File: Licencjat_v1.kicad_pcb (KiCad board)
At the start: 2 copper layers, 53 parts, among them J1 Conn_01x02_Socket, J2 Conn_01x02_Socket, J3 Conn_01x04_Socket, J4 Conn_01x05_Socket, J5 Conn_01x04_Socket, J6 Conn_01x04_Socket, J7 AVR-ISP-6, Q1 AO3401A, Q10 2SC1945, Q2 BC846, Q3 AO3401A, Q4 AO3401A, Q8 AO3401A, Q9 2SC1945, U1 ATmega328P-A, U2 XC6206PxxxMR, U3 HT75xx-1-SOT89, Y1 Crystal_Small

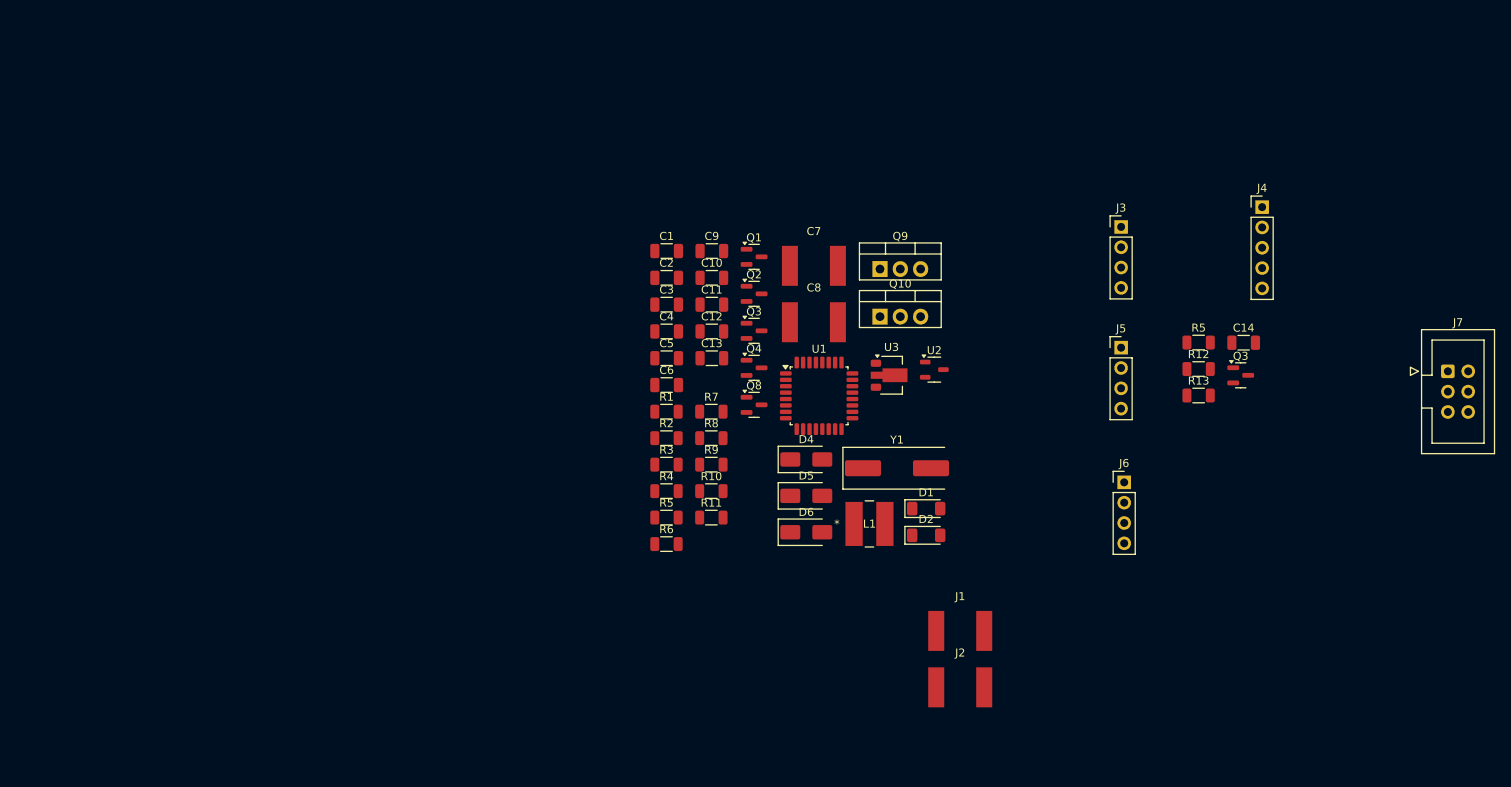
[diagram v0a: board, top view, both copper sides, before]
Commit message: Add 1Wire, RF Level SHifter and better footprints
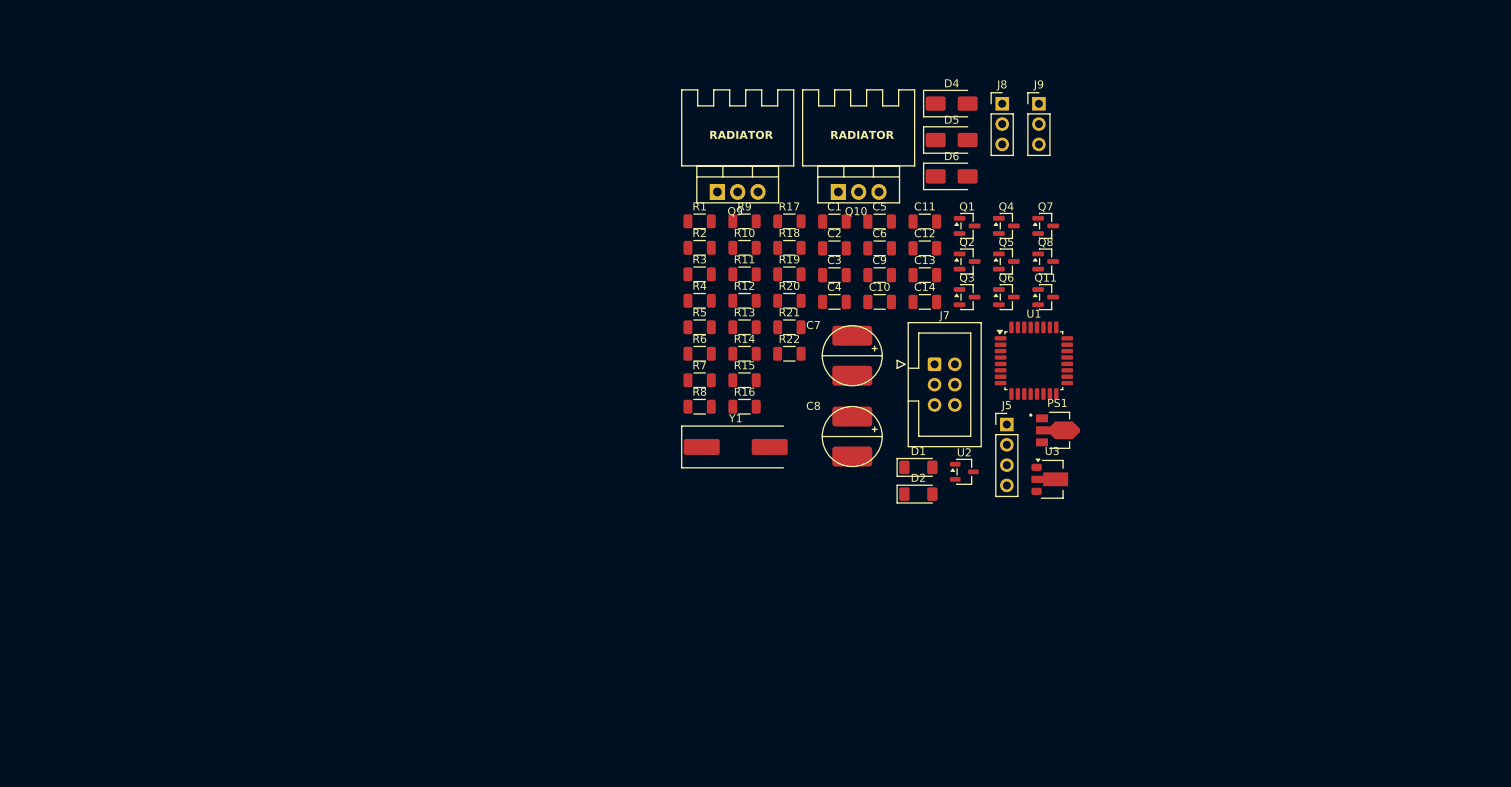
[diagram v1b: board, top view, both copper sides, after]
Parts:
- removed J1, J2: Conn_01x02_Socket, foot_prints:DoubleSolderWirePad_1x01_SMD_2x5mm
- removed J3: Conn_01x04_Socket, foot_prints:ATH20 + BMP280
- removed J4: Conn_01x05_Socket, foot_prints:VEML7700
- removed J6: Conn_01x04_Socket, foot_prints:RF_TRANSMITTER
- removed L1: L, Inductor cd54:IND_CD54_SUM
- removed the Q3 at (163.1, 61.0)
- removed the Q3 at (102.2, 55.4)
- removed the R5 at (157.8, 56.9)
- removed the R5 at (91.3, 78.8)
- added J8: GEIGER, Connector_PinHeader_2.54mm:PinHeader_1x03_P2.54mm_Vertical, F.Cu at (133.2, 27.1)
- added J9: 1_WIRE, Connector_PinHeader_2.54mm:PinHeader_1x03_P2.54mm_Vertical, F.Cu at (137.8, 27.1)
- added PS1: ME2108A33P, ME2108A33P:CONV_ME2108A33P, F.Cu at (140.2, 67.9)
- added Q11: AO3400A, Package_TO_SOT_SMD:SOT-23, F.Cu at (138.7, 51.2)
- added Q3: AO3401A, Package_TO_SOT_SMD:SOT-23, F.Cu at (128.9, 51.2)
- added Q5: AO3400A, Package_TO_SOT_SMD:SOT-23, F.Cu at (133.8, 46.8)
- added Q6: AO3400A, Package_TO_SOT_SMD:SOT-23, F.Cu at (133.8, 51.2)
- added Q7: AO3401A, Package_TO_SOT_SMD:SOT-23, F.Cu at (138.7, 42.3)
- added R14: 10k, Resistor_SMD:R_1206_3216Metric, F.Cu at (101.0, 58.3)
- added R15: 10k, Resistor_SMD:R_1206_3216Metric, F.Cu at (101.0, 61.6)
- added R16: 10k, Resistor_SMD:R_1206_3216Metric, F.Cu at (101.0, 64.9)
- added R17: 47k, Resistor_SMD:R_1206_3216Metric, F.Cu at (106.7, 41.8)
- added R18: 10k, Resistor_SMD:R_1206_3216Metric, F.Cu at (106.7, 45.1)
- added R19: 10k, Resistor_SMD:R_1206_3216Metric, F.Cu at (106.7, 48.4)
- added R20: 10k, Resistor_SMD:R_1206_3216Metric, F.Cu at (106.7, 51.7)
- added R21: 10k, Resistor_SMD:R_1206_3216Metric, F.Cu at (106.7, 55.0)
- added R22: 10k, Resistor_SMD:R_1206_3216Metric, F.Cu at (106.7, 58.3)
- added R5: 10k, Resistor_SMD:R_1206_3216Metric, F.Cu at (95.4, 55.0)
- C10, C11, C5, C6, C9: value C_Small -> 10u
- C12, C13: value C_Small -> 100n
- C14: value C_Small -> 1u
- C7, C8: value C_Polarized -> 500F; footprint foot_prints:DoubleSolderWirePad_1x01_SMD_2x5mm -> Project Elements:Super Capacitor
- J5: value Conn_01x04_Socket -> ADDITIONAL I2C
- Q10, Q9: footprint Package_TO_SOT_THT:TO-220-3_Vertical -> Project Elements:TO-220-3_Vertical+Radiator
- Q4: value AO3401A -> AO3400A
- R12, R13, R3, R4, R6, R9: value R_Small -> 10k
- moved J7 64.2 mm to (124.8, 59.6)
- moved R12 57.4 mm to (101.0, 51.7)
- moved R13 57.4 mm to (101.0, 55.0)
- moved D4 48.0 mm to (126.9, 27.0)
- moved D5 48.0 mm to (126.9, 31.6)
- moved D6 48.0 mm to (126.9, 36.1)
- moved Q8 40.6 mm to (138.7, 46.8)
- moved C14 40.2 mm to (123.6, 51.8)
- moved Q4 36.2 mm to (133.8, 42.3)
- moved C5 31.6 mm to (117.9, 41.8)
- moved C6 31.6 mm to (117.9, 45.1)
- moved R9 30.7 mm to (101.0, 41.8)
- moved R10 30.7 mm to (101.0, 45.1)
- moved R11 30.7 mm to (101.0, 48.4)
- moved C11 28.6 mm to (123.6, 41.8)
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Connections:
- net /GEIGER_VIN renamed /VCC_GEIGER
- C1 pad 2: GND -> ~
- C10 pad 1: GND -> ~
- C11 pad 1: GND -> ~
- C12 pad 1: GND -> ~
- C13 pad 1: GND -> ~
- C14 pad 1: GND -> /D5/T1
- C14 pad 2: Net-(D6-K) -> ~
- C2 pad 2: GND -> ~
- C3 pad 1: GND -> ~
- C4 pad 2: GND -> ~
- C5 pad 2: GND -> ~
- C6 pad 2: GND -> ~
- C8 pad 2: GND -> ~
- C9 pad 1: GND -> ~
- J5 pad 2: /SDA -> /SDA_SHIFTED
- J5 pad 3: GND -> /SCL_SHIFTED
- J5 pad 4: /SCL -> ~
- J7 pad 6: GND -> ~
- Q2 pad 1: /GEIGER_OUT -> /GEIGER_IN
- Q2 pad 2: GND -> ~
- Q2 pad 3: /D5/T1 -> Net-(Q2-C)
- Q4 pad 1: Net-(Q4-G) -> /VCC_I2C
- Q4 pad 2: Net-(Q3-S) -> /SDA_SHIFTED
- Q4 pad 3: Net-(J5-Pin_1) -> /SDA
- Q9 pad 2: GND -> ~
- R11 pad 1: GND -> ~
- R12 pad 2: /VCC_I2C_1 -> /VCC_I2C
- R13 pad 2: /VCC_I2C_1 -> /VCC_I2C
- R4 pad 2: /D5/T1 -> Net-(Q2-C)
- R6 pad 1: Net-(Q4-G) -> /SDA
- R6 pad 2: Net-(Q3-S) -> /VCC
- R8 pad 1: GND -> ~
- U1 pad 21: GND -> ~
- U1 pad 3: GND -> ~
- U1 pad 5: GND -> ~
- U2 pad 1: GND -> ~
- U3 pad 1: GND -> ~

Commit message: Start placing components
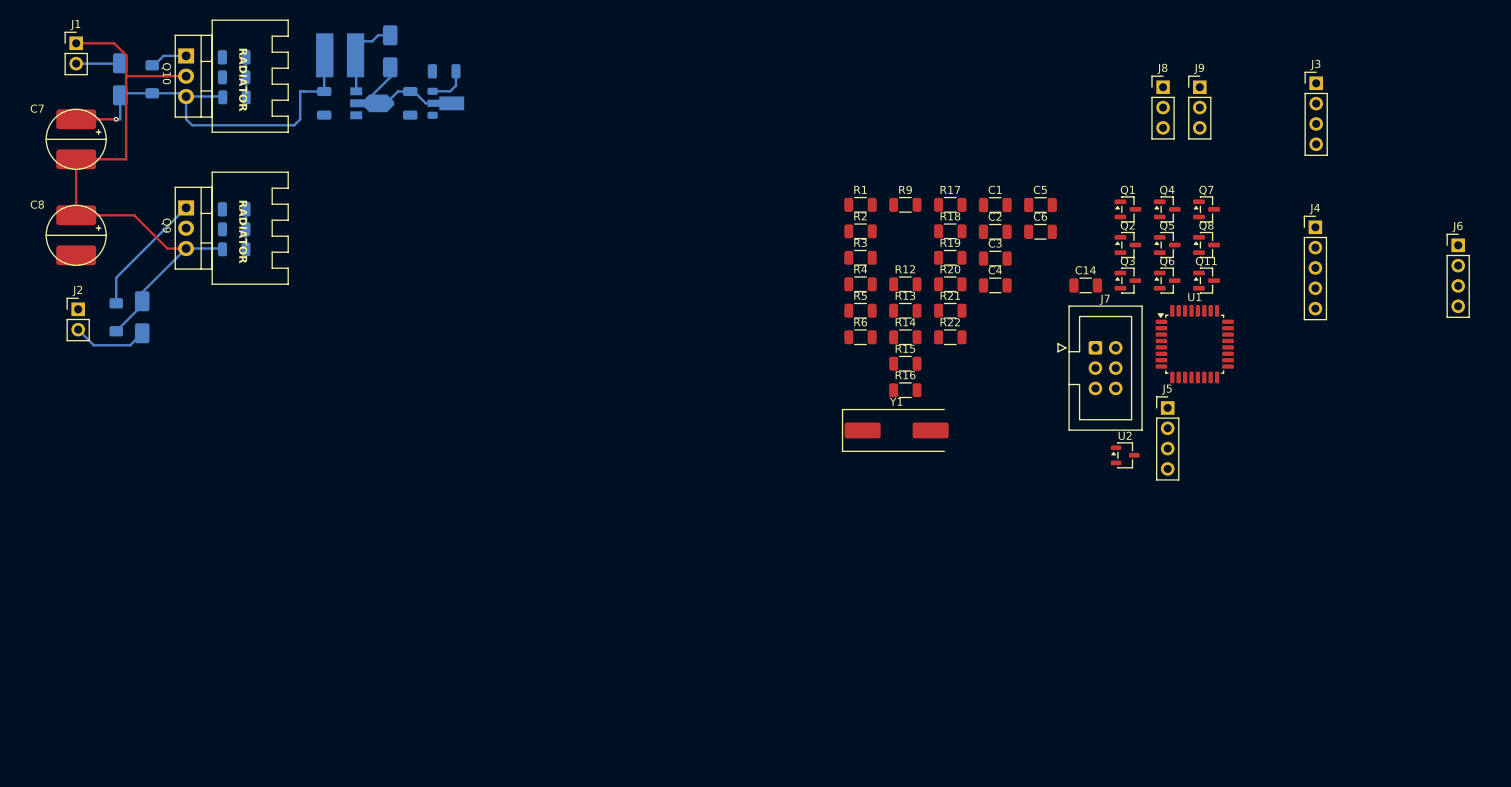
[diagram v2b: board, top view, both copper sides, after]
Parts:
- added J1: PV_IN_1, Connector_PinHeader_2.54mm:PinHeader_1x02_P2.54mm_Vertical, F.Cu at (17.5, 19.5)
- added J2: PV_IN_2, Connector_PinHeader_2.54mm:PinHeader_1x02_P2.54mm_Vertical, F.Cu at (17.8, 52.8)
- added J3: AHT20 + BMP280, Project Modules:ATH20 + BMP280, F.Cu at (172.5, 24.5)
- added J4: VEML7700, Project Modules:VEML7700, F.Cu at (172.4, 42.5)
- added J6: RF_TRANSMITTER, Project Modules:RF_TRANSMITTER, F.Cu at (190.2, 44.8)
- added L1: L, CD54:IND_CD54_SUM, B.Cu at (50.5, 21.0)
- C10, C11, C12, C13, C9, D1, D2, D4, D5, D6, PS1, R10, R11, R7, R8, U3: moved to B.Cu
- moved D1 107.4 mm to (27.0, 24.0), turned to 90 degrees
- moved D4 104.0 mm to (23.0, 24.0), turned to 90 degrees
- moved D5 103.6 mm to (25.8, 53.8), turned to -90 degrees
- moved D2 102.7 mm to (22.5, 53.8), turned to 90 degrees
- moved C7 100.7 mm to (15.0, 27.7)
- moved C8 100.2 mm to (15.0, 39.7)
- moved PS1 95.0 mm to (54.5, 27.0)
- moved C12 89.6 mm to (37.2, 21.2)
- moved U3 88.9 mm to (64.0, 27.0)
- moved C13 86.7 mm to (37.2, 40.2)
- moved Q10 77.4 mm to (34.5, 18.5), turned to -90 degrees
- moved C10 73.7 mm to (48.5, 27.0), turned to 90 degrees
- moved D6 71.9 mm to (56.8, 20.5), turned to 90 degrees
- moved R8 71.3 mm to (37.2, 23.8)
- moved R7 68.1 mm to (37.3, 26.2), turned to 180 degrees
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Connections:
- C1 pad 2: ~ -> GND
- C10 pad 1: ~ -> GND
- C11 pad 1: ~ -> GND
- C13 pad 1: ~ -> GND
- C14 pad 2: ~ -> GND
- C2 pad 2: ~ -> GND
- C3 pad 1: ~ -> GND
- C4 pad 2: ~ -> GND
- C5 pad 2: ~ -> GND
- C6 pad 2: ~ -> GND
- C8 pad 2: ~ -> GND
- C9 pad 1: ~ -> GND
- J5 pad 4: ~ -> GND
- J7 pad 6: ~ -> GND
- J8 pad 3: ~ -> GND
- J9 pad 3: ~ -> GND
- PS1 pad 1: ~ -> GND
- Q2 pad 2: ~ -> GND
- Q9 pad 2: ~ -> GND
- R11 pad 1: ~ -> GND
- U1 pad 21: ~ -> GND
- U1 pad 3: ~ -> GND
- U1 pad 5: ~ -> GND
- U2 pad 1: ~ -> GND
- U3 pad 1: ~ -> GND
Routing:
- net /V_HALF_CAP: track 0.00 -> 74.8 mm
- net /V_CAP: track 0.00 -> 51.0 mm, vias 0 -> 1
- net Net-(D6-K): track 0.00 -> 17.7 mm
- net Net-(D2-A): track 0.00 -> 15.6 mm
- net Net-(D6-A): track 0.00 -> 10.9 mm
- net Net-(D5-A): track 0.00 -> 9.43 mm
- net Net-(D4-A): track 0.00 -> 5.52 mm
- net /A0: track 0.00 -> 5.02 mm
- net /A1: track 0.00 -> 5.01 mm
- net /VCC: track 0.00 -> 5.00 mm
- net Net-(D1-A): track 0.00 -> 4.73 mm

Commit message: Component placing continues
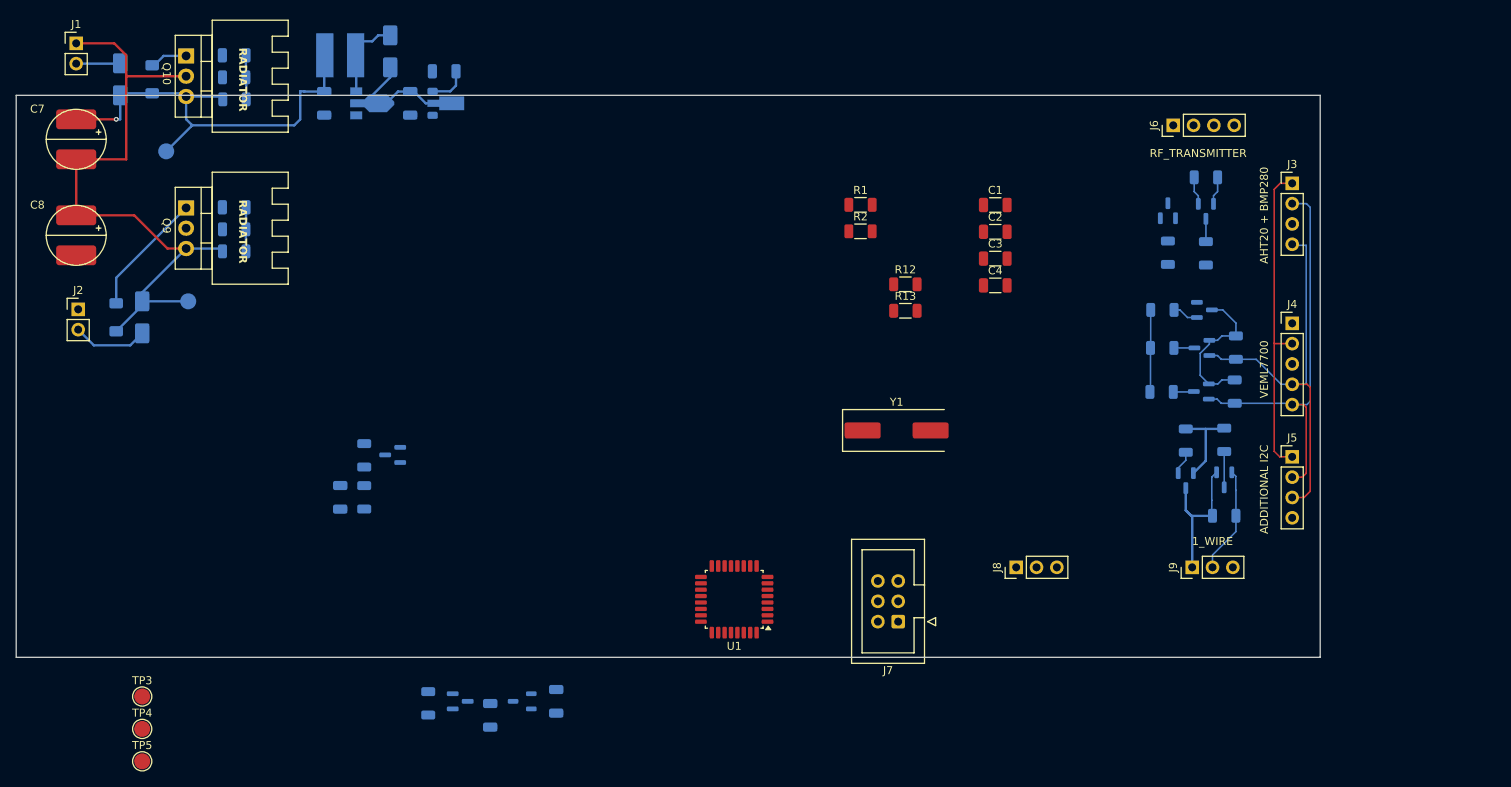
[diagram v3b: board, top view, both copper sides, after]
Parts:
- added TP1: V_HALF_CAP_TP, TestPoint:TestPoint_Pad_D2.0mm, B.Cu at (31.5, 51.8)
- added TP2: V_CAP_TP, TestPoint:TestPoint_Pad_D2.0mm, B.Cu at (28.8, 33.0)
- added TP3: V_BOOST_TP, TestPoint:TestPoint_Pad_D2.0mm, F.Cu at (25.8, 101.2)
- added TP4: VCC_TP, TestPoint:TestPoint_Pad_D2.0mm, F.Cu at (25.8, 105.2)
- added TP5: VCC_GEIGER_TP, TestPoint:TestPoint_Pad_D2.0mm, F.Cu at (25.8, 109.2)
- C14, C5, C6, Q1, Q11, Q2, Q3, Q4, Q5, Q6, Q7, Q8, R14, R15, R16, R17, R18, R19, R20, R21, R22, R3, R4, R5, R6, R9, U2: moved to B.Cu
- moved Q1 103.7 mm to (65.5, 101.8)
- moved C14 96.9 mm to (50.5, 76.2), turned to -90 degrees
- moved Q2 95.6 mm to (57.1, 71.0), turned to 180 degrees
- moved C5 93.8 mm to (69.2, 103.5), turned to -90 degrees
- moved C6 84.3 mm to (77.5, 101.8), turned to 90 degrees
- moved R17 81.9 mm to (53.5, 76.2), turned to 90 degrees
- moved U2 81.4 mm to (73.2, 101.8), turned to 180 degrees
- moved R3 77.6 mm to (61.5, 102.0), turned to 90 degrees
- moved U1 65.8 mm to (99.8, 89.0), turned to 180 degrees
- moved R4 65.6 mm to (53.5, 71.0), turned to -90 degrees
- moved J8 62.8 mm to (135.0, 85.0), turned to 90 degrees
- moved J9 60.0 mm to (157.0, 85.0), turned to 90 degrees
- moved R19 47.0 mm to (161.0, 78.6), turned to 180 degrees
- moved R18 43.0 mm to (161.0, 69.1), turned to 90 degrees
- moved J7 42.2 mm to (120.2, 91.8), turned to 180 degrees
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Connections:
- C12 pad 1: ~ -> GND
- J4 pad 2: /VCC_I2C_1 -> /VCC_I2C
- J5 pad 1: /VCC_I2C_1 -> /VCC_I2C
- Q8 pad 3: /VCC_I2C_1 -> /VCC_I2C
- R8 pad 1: ~ -> GND
- U1 pad 1: /D3 -> /1_WIRE
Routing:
- net /VCC_I2C: track 0.00 -> 58.8 mm
- net /SDA_SHIFTED: track 0.00 -> 51.9 mm
- net /SCL_SHIFTED: track 0.00 -> 50.7 mm
- net /VCC: track 5.00 -> 26.3 mm
- net /VCC_1_WIRE: track 0.00 -> 19.7 mm
- net /1_WIRE_SHIFTED: track 0.00 -> 13.7 mm
- net /V_HALF_CAP: track 74.8 -> 80.3 mm
- net /V_CAP: track 51.0 -> 55.7 mm
- net /1_WIRE: track 0.00 -> 4.47 mm
- net /RF_DATA_SHIFTED: track 0.00 -> 3.52 mm
- net /VCC_RF: track 0.00 -> 3.52 mm
- net /D6: track 0.00 -> 3.24 mm
- net /~{EN_VCC_1_WIRE}: track 0.00 -> 2.99 mm
- net /D10: track 0.00 -> 2.85 mm
- net /SDA: track 0.00 -> 2.58 mm
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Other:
- board outline added: 163 x 70.2 mm
- board text added: "V_CAP"
- board text added: "V_HALF_CAP"

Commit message: Component placing
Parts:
- moved C14 12.2 mm to (58.1, 85.8)
- moved Q2 12.2 mm to (64.7, 80.5)
- moved R17 12.2 mm to (61.1, 85.8)
- moved R4 12.2 mm to (61.1, 80.5)
- moved J4 10.7 mm to (169.0, 65.2), turned to 180 degrees
- moved R6 9.44 mm to (149.2, 54.5)
- moved J3 9.01 mm to (169.0, 46.0), turned to 180 degrees
- moved Q4 8.71 mm to (156.4, 54.5)
- moved R14 8.56 mm to (161.8, 54.5)
- moved R15 7.65 mm to (149.1, 64.0)
- moved R9 7.65 mm to (149.1, 59.2)
- moved Q5 6.29 mm to (156.1, 63.5)
- moved Q8 6.29 mm to (156.4, 58.8)
- moved R16 4.52 mm to (161.7, 62.0)
- moved R19 3.05 mm to (158.0, 79.1)
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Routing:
- net /RF_DATA_SHIFTED: track 3.52 -> 17.5 mm
- net /VCC_RF: track 3.52 -> 17.1 mm
- net /SCL_SHIFTED: track 50.7 -> 56.0 mm
- net /VCC_I2C: track 58.8 -> 54.0 mm
- net /VCC: track 26.3 -> 30.7 mm
- net /VCC_1_WIRE: track 19.7 -> 15.8 mm
- net /D7: track 0.00 -> 3.24 mm
- net /SDA: track 2.58 -> 4.87 mm
- net /SCL: track 2.56 -> 4.81 mm
- net /SDA_SHIFTED: track 51.9 -> 49.7 mm
- net /1_WIRE: track 4.47 -> 6.65 mm
- net /D6: track 3.24 -> 5.07 mm
- net /~{EN_VCC_1_WIRE}: track 2.99 -> 4.37 mm
- net /1_WIRE_SHIFTED: track 13.7 -> 12.4 mm

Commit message: Elements placed
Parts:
- removed R12, R13: 10k, Resistor_SMD:R_1206_3216Metric
- added J10: SERIAL, Connector_PinHeader_2.54mm:PinHeader_1x04_P2.54mm_Vertical, F.Cu at (139.1, 29.8)
- C1, C2, C3, C4, R1, R2, TP3, TP4, TP5, U1, Y1: moved to B.Cu
- moved TP5 110.1 mm to (131.7, 79.2), turned to 180 degrees
- moved TP4 107.0 mm to (118.1, 51.2), turned to 180 degrees
- moved TP3 101.5 mm to (114.1, 51.2), turned to 180 degrees
- moved C14 94.0 mm to (152.0, 80.0), turned to 90 degrees
- moved R3 87.5 mm to (143.8, 72.2), turned to 180 degrees
- moved R17 87.3 mm to (148.2, 80.0)
- moved Q1 85.2 mm to (143.8, 68.0), turned to 90 degrees
- moved C13 84.7 mm to (117.0, 68.5)
- moved C8 84.7 mm to (94.8, 68.2)
- moved D2 84.7 mm to (102.3, 82.2)
- moved D5 84.7 mm to (105.5, 82.2)
- moved J2 84.7 mm to (97.5, 81.2)
- moved Q9 84.7 mm to (114.3, 66.0)
- moved R10 84.7 mm to (117.0, 74.0)
- moved R11 84.7 mm to (117.0, 71.2)
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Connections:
- C12 pad 2: /A0 -> /A1
- C13 pad 2: /A1 -> /A0
- Q7 pad 1: /~{EN_VCC_1_WIRE} -> /D8
- R10 pad 1: /A1 -> /A0
- R11 pad 2: /A1 -> /A0
- R20 pad 1: /~{EN_VCC_1_WIRE} -> /D8
- R7 pad 1: /A0 -> /A1
- R8 pad 2: /A0 -> /A1
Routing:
- net /VCC: track 30.7 -> 110.4 mm
- net /A0: track 5.02 -> 35.5 mm, vias 0 -> 2
- net /D11/MOSI: track 0.00 -> 26.9 mm
- net /RX: track 0.00 -> 21.7 mm
- net /V_CAP: track 55.7 -> 34.5 mm
- net Net-(U1-XTAL1/PB6): track 0.00 -> 21.0 mm
- net /D13/SCK: track 0.00 -> 20.2 mm
- net /D12/MISO: track 0.00 -> 19.7 mm
- net Net-(U1-XTAL2/PB7): track 0.00 -> 15.9 mm
- net /VCC_GEIGER: track 0.00 -> 15.6 mm
- net /TX: track 0.00 -> 14.1 mm
- net Net-(Q1-D): track 0.00 -> 12.7 mm
- net /GEIGER_IN: track 0.00 -> 10.6 mm
- net Net-(Q2-C): track 0.00 -> 9.12 mm
- net /D1/TX: track 0.00 -> 6.87 mm
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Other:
- board size 163 x 70.2 mm -> 163 x 65 mm
